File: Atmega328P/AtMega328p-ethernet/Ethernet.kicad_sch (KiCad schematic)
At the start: 35 parts, among them J3 RJ45_Abracon_ARJP11A-MASA-B-A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, U2 W5500, Y2 25MHz

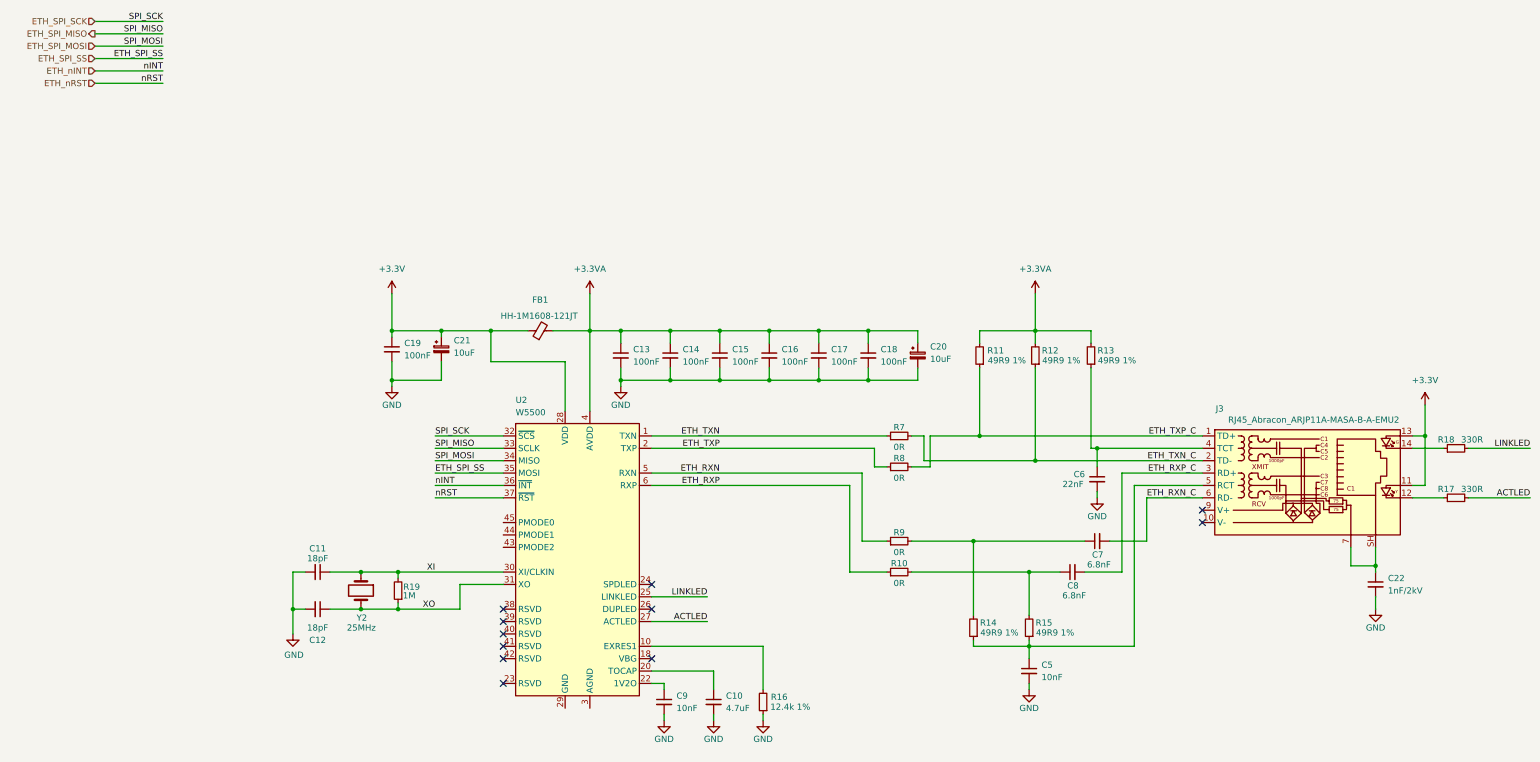
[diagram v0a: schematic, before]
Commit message: Most components selected using lcsc
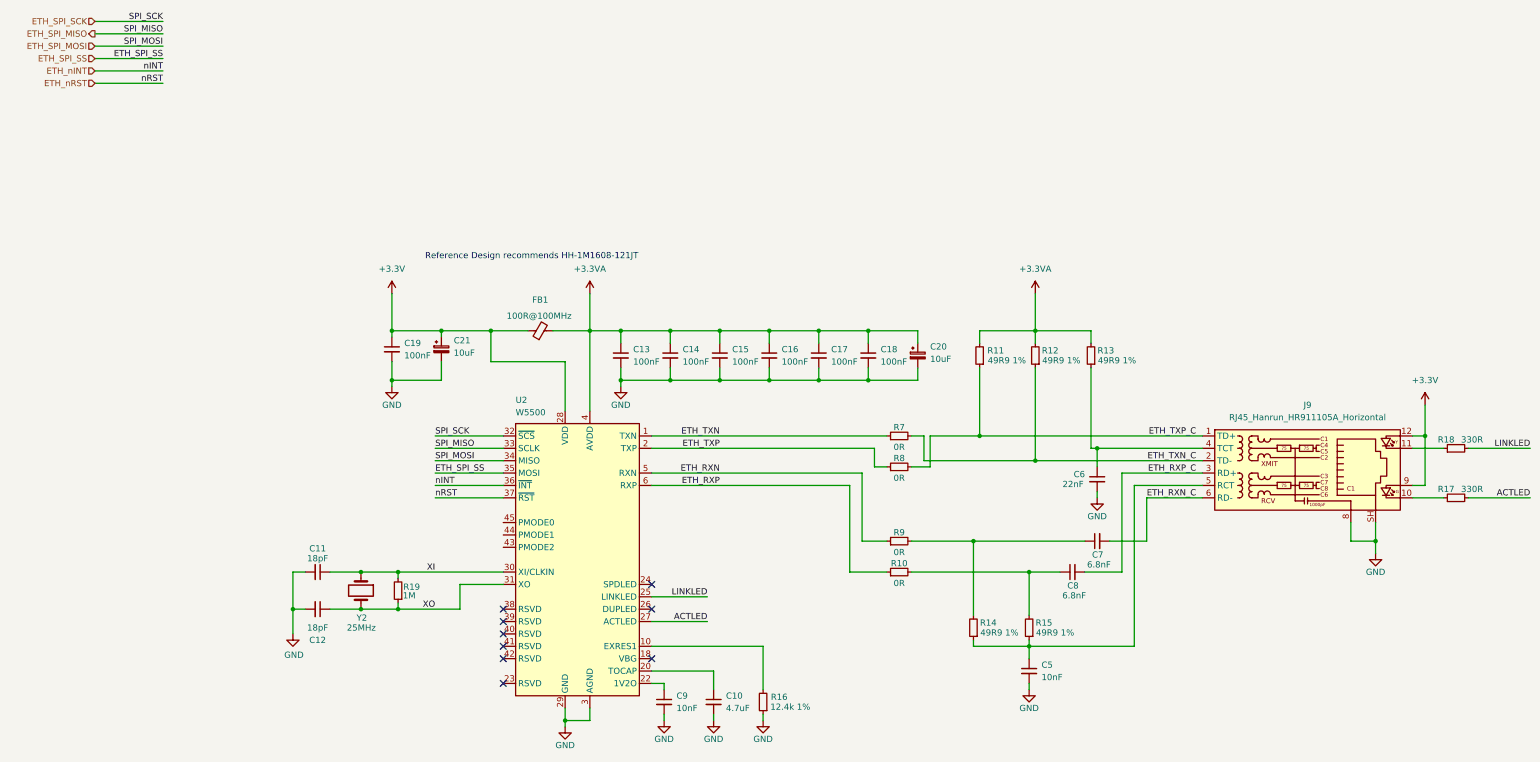
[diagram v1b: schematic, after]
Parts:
- removed C22: 1nF/2kV, Capacitor_SMD:C_0603_1608Metric, symbol Device:C_Small
- removed J3: RJ45_Abracon_ARJP11A-MASA-B-A-EMU2, Connector_RJ:RJ45_Abracon_ARJP11A-MA_Horizontal, symbol Connector:RJ45_Abracon_ARJP11A-MASA-B-A-EMU2
- added J9: RJ45_Hanrun_HR911105A_Horizontal, Connector_RJ:RJ45_Hanrun_HR911105A_Horizontal, symbol Connector:RJ45_Hanrun_HR911105A_Horizontal
- C10, C20, C21: footprint Capacitor_SMD:CP_Elec_4x3 -> Capacitor_SMD:C_1206_3216Metric
- FB1: value HH-1M1608-121JT -> 100R@100MHz
- R10, R7, R8, R9: footprint Resistor_SMD:R_0603_1608Metric -> Resistor_SMD:R_0805_2012Metric_Pad1.20x1.40mm_HandSolder
- Y2: footprint Crystal:Crystal_SMD_2012-2Pin_2.0x1.2mm -> Crystal:Crystal_SMD_3225-4Pin_3.2x2.5mm
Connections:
- net +3.3V: now also J9.12, J9.9
- net ETH_RXN_C: now also J9.6 (RD-)
- net ETH_RXP_C: now also J9.3 (RD+)
- net ETH_TXN_C: now also J9.2 (TD-)
- net ETH_TXP_C: now also J9.1 (TD+)
- net GND: now also U2.14 (AGND), U2.16 (AGND), U2.19 (AGND), U2.29 (GND), U2.3 (AGND), U2.48 (AGND), U2.9 (AGND), J9.8, J9.SH
- net at R18.1: now also J9.11
- net at C6.1, R13.1: now also J9.4 (TCT)
- net at C5.1, R14.1, R15.1: now also J9.5 (RCT)
- net at R17.1: now also J9.10
- no-connect marks 11 -> 9
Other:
- note added: "Reference Design recommends HH-1M1608-121JT"

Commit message: Continued cleanup
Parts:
- removed FB1: 100R@100MHz, Inductor_SMD:L_0603_1608Metric, symbol Device:FerriteBead_Small
- added C22: 1000pF, Capacitor_SMD:C_0603_1608Metric, symbol Device:C_Small
- added R20, R24, R25: 0R, Resistor_SMD:R_0805_2012Metric_Pad1.20x1.40mm_HandSolder, symbol Device:R_Small
- R16: footprint Resistor_SMD:R_0603_1608Metric -> Resistor_SMD:R_0603_1608Metric_Pad0.98x0.95mm_HandSolder; now left out of the parts list
- Y2: symbol Device:Crystal -> Device:Crystal_GND24
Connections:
- net GND: now also C22.2, R20.1, R24.1, R25.1; no longer J9.8, J9.SH
- net XO: now also Y2.3; no longer Y2.2
- net at U2.43 (PMODE2): now also R25.2
- net at U2.44 (PMODE1): now also R24.2
- net at U2.45 (PMODE0): now also R20.2
- net +3.3V renamed +3.3V_IN
- net +3.3VA renamed +3.3VA_IN
- new net: C22.1, J9.8, J9.SH
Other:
- note removed: "Reference Design recommends HH-1M1608-121JT"
- moved on the sheet: C19, C21

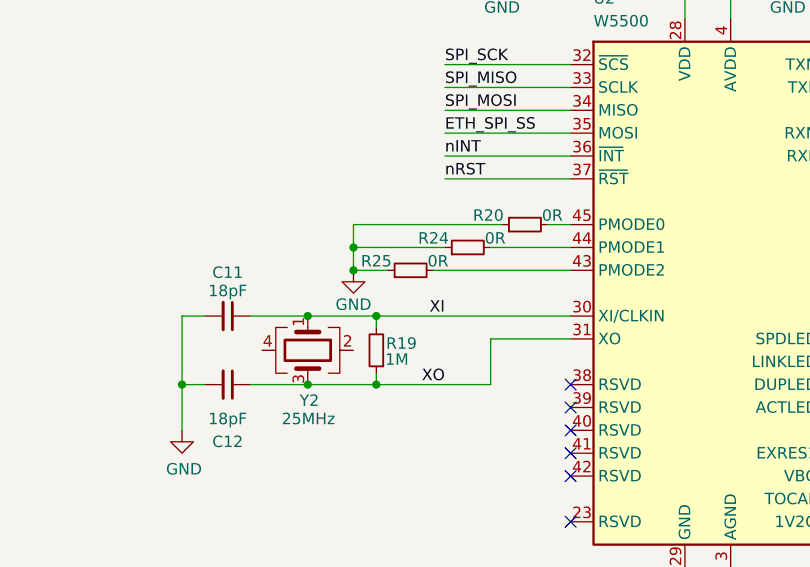
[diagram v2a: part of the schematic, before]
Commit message: Most components layed out and locked still to do ethernet
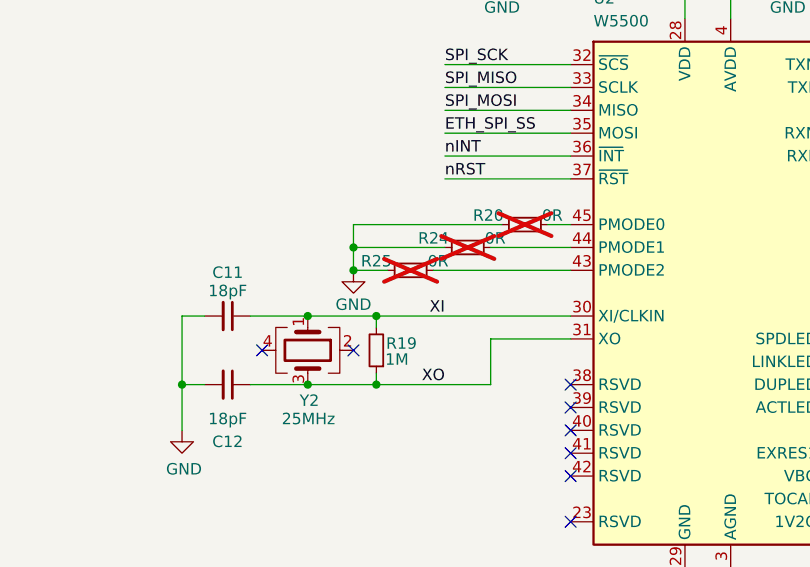
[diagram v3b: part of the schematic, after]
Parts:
- R20, R24, R25: now not fitted
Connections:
- no-connect marks 9 -> 11
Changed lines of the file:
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@@
 	)
 	(no_connect
+		(at 99.06 149.86)
+	)
+	(no_connect
 		(at 133.35 158.75)
 	)
@@
 	)
 	(no_connect
+		(at 109.22 149.86)
+	)
+	(no_connect
 		(at 133.35 156.21)
 	)
@@
 		(in_bom yes)
 		(on_board yes)
-		(dnp no)
+		(dnp yes)
 		(property "Reference" "R20"
 			(at 124.206 134.874 90)
@@
 		(in_bom yes)
 		(on_board yes)
-		(dnp no)
+		(dnp yes)
 		(property "Reference" "R25"
 			(at 111.76 139.954 90)
@@
 		(in_bom yes)
 		(on_board yes)
-		(dnp no)
+		(dnp yes)
 		(property "Reference" "R24"
 			(at 118.11 137.414 90)

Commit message: Layout complete ready for review
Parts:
- C10: footprint Capacitor_SMD:C_1206_3216Metric -> Capacitor_SMD:C_0805_2012Metric; LCSC C29823 -> C1779
- R16: footprint Resistor_SMD:R_0603_1608Metric_Pad0.98x0.95mm_HandSolder -> Resistor_SMD:R_0805_2012Metric_Pad1.20x1.40mm_HandSolder
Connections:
- net ETH_RXN renamed ETH_RX_N
- net ETH_RXN_C renamed ETH_C_RX_N
- net ETH_RXP renamed ETH_RX_P
- net ETH_RXP_C renamed ETH_C_RX_P
- net ETH_TXN renamed ETH_TX_N
- net ETH_TXN_C renamed ETH_C_TX_N
- net ETH_TXP renamed ETH_TX_P
- net ETH_TXP_C renamed ETH_C_TX_P
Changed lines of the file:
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@@
 		)
 	)
-	(label "ETH_TXP_C"
+	(label "ETH_C_TX_P"
 		(at 275.59 118.11 180)
 		(effects
@@
 		)
 	)
-	(label "ETH_TXP"
+	(label "ETH_TX_P"
 		(at 177.8 120.65 180)
 		(effects
@@
 		)
 	)
-	(label "ETH_RXN_C"
+	(label "ETH_C_RX_N"
 		(at 275.59 130.81 180)
 		(effects
@@
 		)
 	)
-	(label "ETH_RXN"
+	(label "ETH_RX_N"
 		(at 177.8 125.73 180)
 		(effects
@@
 		)
 	)
-	(label "ETH_TXN"
+	(label "ETH_TX_N"
 		(at 177.8 118.11 180)
 		(effects
@@
 		)
 	)
-	(label "ETH_RXP"
+	(label "ETH_RX_P"
 		(at 177.8 128.27 180)
 		(effects
@@
 		)
 	)
-	(label "ETH_RXP_C"
+	(label "ETH_C_RX_P"
 		(at 275.59 125.73 180)
 		(effects
@@
 		)
 	)
-	(label "ETH_TXN_C"
+	(label "ETH_C_TX_N"
 		(at 275.59 123.19 180)
 		(effects
@@
 			)
 		)
-		(property "Footprint" "Capacitor_SMD:C_1206_3216Metric"
+		(property "Footprint" "Capacitor_SMD:C_0805_2012Metric"
 			(at 176.53 172.72 0)
 			(effects
@@
 			)
 		)
-		(property "LCSC" "C29823"
+		(property "LCSC" "C1779"
 			(at 176.53 172.72 0)
 			(effects
@@
 			)
 		)
-		(property "Footprint" "Resistor_SMD:R_0603_1608Metric_Pad0.98x0.95mm_HandSolder"
+		(property "Footprint" "Resistor_SMD:R_0805_2012Metric_Pad1.20x1.40mm_HandSolder"
 			(at 186.69 172.72 0)
 			(effects

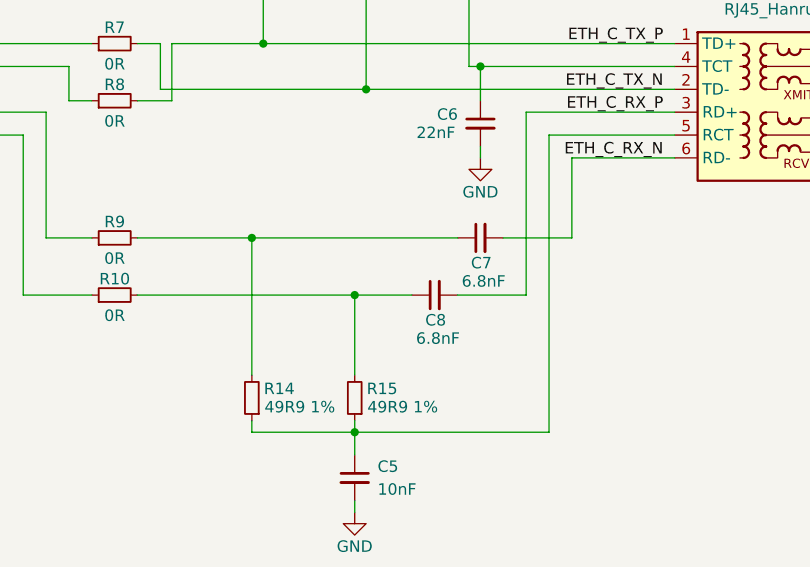
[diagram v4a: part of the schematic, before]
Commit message: Most traces complete just GPIO left
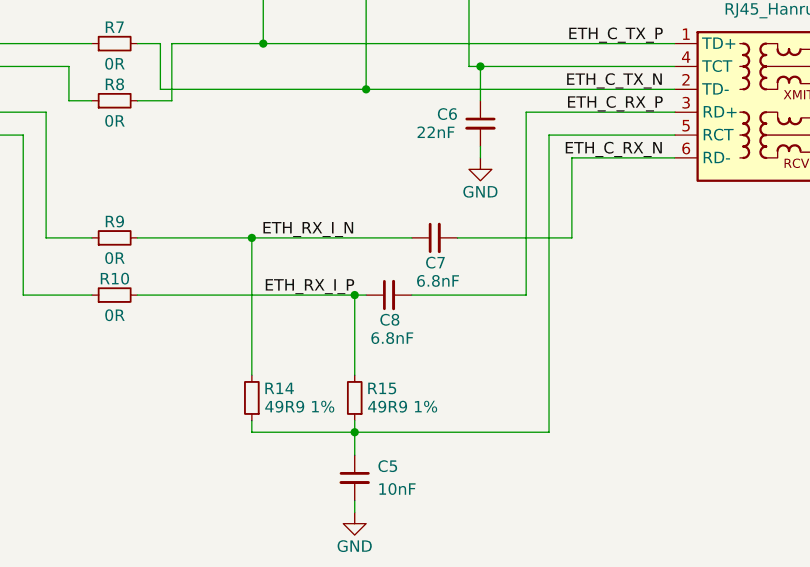
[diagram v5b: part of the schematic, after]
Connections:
- net ETH_RX_I_P: now reaches C8.1, R10.2, R15.2
- net ETH_RX_I_N: now reaches C7.1, R14.2, R9.2
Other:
- moved on the sheet: C7, C8
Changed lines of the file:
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@@
+	(wire
+		(pts
+			(xy 229.87 139.7) (xy 247.65 139.7)
+		)
+		(stroke
+			(width 0)
+			(type default)
+		)
+	)
 	(wire
 		(pts
@@
 	(wire
 		(pts
-			(xy 252.73 146.05) (xy 260.35 146.05)
+			(xy 247.65 146.05) (xy 260.35 146.05)
 		)
 		(stroke
@@
 	(wire
 		(pts
-			(xy 257.81 139.7) (xy 265.43 139.7)
+			(xy 252.73 139.7) (xy 265.43 139.7)
 		)
 		(stroke
@@
 	(wire
 		(pts
-			(xy 229.87 139.7) (xy 252.73 139.7)
-		)
-		(stroke
-			(width 0)
-			(type default)
-		)
-	)
-	(wire
-		(pts
 			(xy 177.8 104.14) (xy 177.8 106.68)
 		)
@@
 	(wire
 		(pts
-			(xy 241.3 146.05) (xy 247.65 146.05)
+			(xy 241.3 146.05) (xy 242.57 146.05)
 		)
 		(stroke
@@
 	(label "ETH_SPI_SS"
 		(at 63.5 40.64 180)
+		(effects
+			(font
+				(size 1.27 1.27)
+			)
+			(justify right bottom)
+		)
+	)
+	(label "ETH_RX_I_P"
+		(at 241.3 146.05 180)
+		(effects
+			(font
+				(size 1.27 1.27)
+			)
+			(justify right bottom)
+		)
+	)
+	(label "ETH_RX_I_N"
+		(at 241.3 139.7 180)
 		(effects
 			(font
@@
 			(fill
 				(type none)
+			)
+		)
+	)
+	(rule_area
+		(polyline
+			(pts
+				(xy 261.62 110.49) (xy 261.62 141.605) (xy 276.86 141.605) (xy 276.86 110.49)
+			)
+			(stroke
+				(width 0)
+				(type dash)
+			)
+			(fill
+				(type none)
+			)
+		)
+	)
+	(rule_area
+		(polyline
+			(pts
+				(xy 223.52 137.16) (xy 223.52 149.86) (xy 242.57 149.86) (xy 242.57 137.16)
+			)
+			(stroke
+				(width 0)
+				(type dash)
+			)
+			(fill
+				(type none)
+			)
+		)
+	)
+	(netclass_flag ""
+		(length 2.54)
+		(shape round)
+		(at 269.24 110.49 0)
+		(fields_autoplaced yes)
+		(effects
+			(font
+				(size 1.27 1.27)
+			)
+			(justify left bottom)
+		)
+		(property "Netclass" "ETHERNET"
+			(at 269.9385 107.95 0)
+			(effects
+				(font
+					(size 1.27 1.27)
+				)
+				(justify left)
+			)
+		)
+		(property "Component Class" ""
+			(at 260.35 60.96 0)
+			(effects
+				(font
+					(size 1.27 1.27)
+					(italic yes)
+				)
 			)
 		)
@@
 		(property "Component Class" ""
 			(at 181.61 67.31 0)
+			(effects
+				(font
+					(size 1.27 1.27)
+					(italic yes)
+				)
+			)
+		)
+	)
+	(netclass_flag ""
+		(length 2.54)
+		(shape round)
+		(at 224.79 137.16 0)
+		(fields_autoplaced yes)
+		(effects
+			(font
+				(size 1.27 1.27)
+			)
+			(justify left bottom)
+		)
+		(property "Netclass" "ETHERNET"
+			(at 225.4885 134.62 0)
+			(effects
+				(font
+					(size 1.27 1.27)
+				)
+				(justify left)
+			)
+		)
+		(property "Component Class" ""
+			(at 215.9 87.63 0)
 			(effects
 				(font
@@
 	(symbol
 		(lib_id "Device:C_Small")
-		(at 250.19 146.05 90)
+		(at 245.11 146.05 90)
 		(unit 1)
 		(exclude_from_sim no)
@@
 		(dnp no)
 		(property "Reference" "C8"
-			(at 251.46 148.844 90)
+			(at 246.38 148.844 90)
 			(effects
 				(font
@@
 		)
 		(property "Value" "6.8nF"
-			(at 252.984 150.876 90)
+			(at 247.904 150.876 90)
 			(effects
 				(font
@@
 		)
 		(property "Footprint" "Capacitor_SMD:C_0603_1608Metric"
-			(at 250.19 146.05 0)
+			(at 245.11 146.05 0)
 			(effects
 				(font
@@
 		)
 		(property "Datasheet" "~"
-			(at 250.19 146.05 0)
+			(at 245.11 146.05 0)
 			(effects
 				(font
@@
 		)
 		(property "Description" "Unpolarized capacitor, small symbol"
-			(at 250.19 146.05 0)
+			(at 245.11 146.05 0)
 			(effects
 				(font
@@
 		)
 		(property "LCSC" "C1631"
-			(at 250.19 146.05 0)
+			(at 245.11 146.05 0)
 			(effects
 				(font
@@
 	(symbol
 		(lib_id "Device:C_Small")
-		(at 255.27 139.7 90)
+		(at 250.19 139.7 90)
 		(unit 1)
 		(exclude_from_sim no)
@@
 		(dnp no)
 		(property "Reference" "C7"
-			(at 256.54 142.494 90)
+			(at 251.46 142.494 90)
 			(effects
 				(font
@@
 		)
 		(property "Value" "6.8nF"
-			(at 258.064 144.526 90)
+			(at 252.984 144.526 90)
 			(effects
 				(font
@@
 		)
 		(property "Footprint" "Capacitor_SMD:C_0603_1608Metric"
-			(at 255.27 139.7 0)
+			(at 250.19 139.7 0)
 			(effects
 				(font
@@
 		)
 		(property "Datasheet" "~"
-			(at 255.27 139.7 0)
+			(at 250.19 139.7 0)
 			(effects
 				(font
@@
 		)
 		(property "Description" "Unpolarized capacitor, small symbol"
-			(at 255.27 139.7 0)
+			(at 250.19 139.7 0)
 			(effects
 				(font
@@
 		)
 		(property "LCSC" "C1631"
-			(at 255.27 139.7 0)
-			(effects
-				(font
+			(at 250.19 139.7 0)
+			(effects
+				(font

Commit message: Ethernet atmega328p reviewed
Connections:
- net ETH_SPI_MISO: now also U2.34 (MISO); no longer U2.33 (SCLK)
- net ETH_SPI_MOSI: now also U2.35 (MOSI); no longer U2.34 (MISO)
- net ETH_SPI_SCK: now also U2.33 (SCLK); no longer U2.32 (~{SCS})
- net ETH_SPI_SS: now also U2.32 (~{SCS}); no longer U2.35 (MOSI)
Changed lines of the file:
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@@
-		)
-	)
-	(label "ETH_SPI_SS"
-		(at 119.38 125.73 0)
-		(effects
-			(font
-				(size 1.27 1.27)
-			)
-			(justify left bottom)
 		)
 	)
@@
 		)
 	)
-	(label "SPI_MOSI"
-		(at 119.38 123.19 0)
-		(effects
-			(font
-				(size 1.27 1.27)
-			)
-			(justify left bottom)
-		)
-	)
 	(label "ETH_C_RX_P"
 		(at 275.59 125.73 180)
@@
 		)
 	)
+	(label "ETH_SPI_SS"
+		(at 119.38 118.11 0)
+		(effects
+			(font
+				(size 1.27 1.27)
+			)
+			(justify left bottom)
+		)
+	)
 	(label "SPI_MISO"
 		(at 63.5 35.56 180)
@@
 		)
 	)
-	(label "SPI_MISO"
-		(at 119.38 120.65 0)
+	(label "SPI_MOSI"
+		(at 119.38 125.73 0)
 		(effects
 			(font
@@
 		)
 	)
+	(label "SPI_MISO"
+		(at 119.38 123.19 0)
+		(effects
+			(font
+				(size 1.27 1.27)
+			)
+			(justify left bottom)
+		)
+	)
 	(label "SPI_SCK"
-		(at 119.38 118.11 0)
+		(at 119.38 120.65 0)
 		(effects
 			(font
@@
 			)
 			(justify left)
+		)
+	)
+	(rule_area
+		(polyline
+			(pts
+				(xy 261.62 110.49) (xy 261.62 141.605) (xy 276.86 141.605) (xy 276.86 110.49)
+			)
+			(stroke
+				(width 0)
+				(type dash)
+			)
+			(fill
+				(type none)
+			)
+		)
+	)
+	(rule_area
+		(polyline
+			(pts
+				(xy 223.52 137.16) (xy 223.52 149.86) (xy 242.57 149.86) (xy 242.57 137.16)
+			)
+			(stroke
+				(width 0)
+				(type dash)
+			)
+			(fill
+				(type none)
+			)
 		)
 	)
@@
 			)
 			(stroke
-				(width 0)
-				(type dash)
-			)
-			(fill
-				(type none)
-			)
-		)
-	)
-	(rule_area
-		(polyline
-			(pts
-				(xy 223.52 137.16) (xy 223.52 149.86) (xy 242.57 149.86) (xy 242.57 137.16)
-			)
-			(stroke
-				(width 0)
-				(type dash)
-			)
-			(fill
-				(type none)
-			)
-		)
-	)
-	(rule_area
-		(polyline
-			(pts
-				(xy 261.62 110.49) (xy 261.62 141.605) (xy 276.86 141.605) (xy 276.86 110.49)
-			)
-			(stroke
